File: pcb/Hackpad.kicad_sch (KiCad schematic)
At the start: 21 parts, among them SW1 SW_Push, SW10 RotaryEncoder, SW2 SW_Push, SW3 SW_Push, SW4 SW_Push, SW5 SW_Push, SW6 SW_Push, SW7 SW_Push, SW8 SW_Push, SW9 SW_Push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

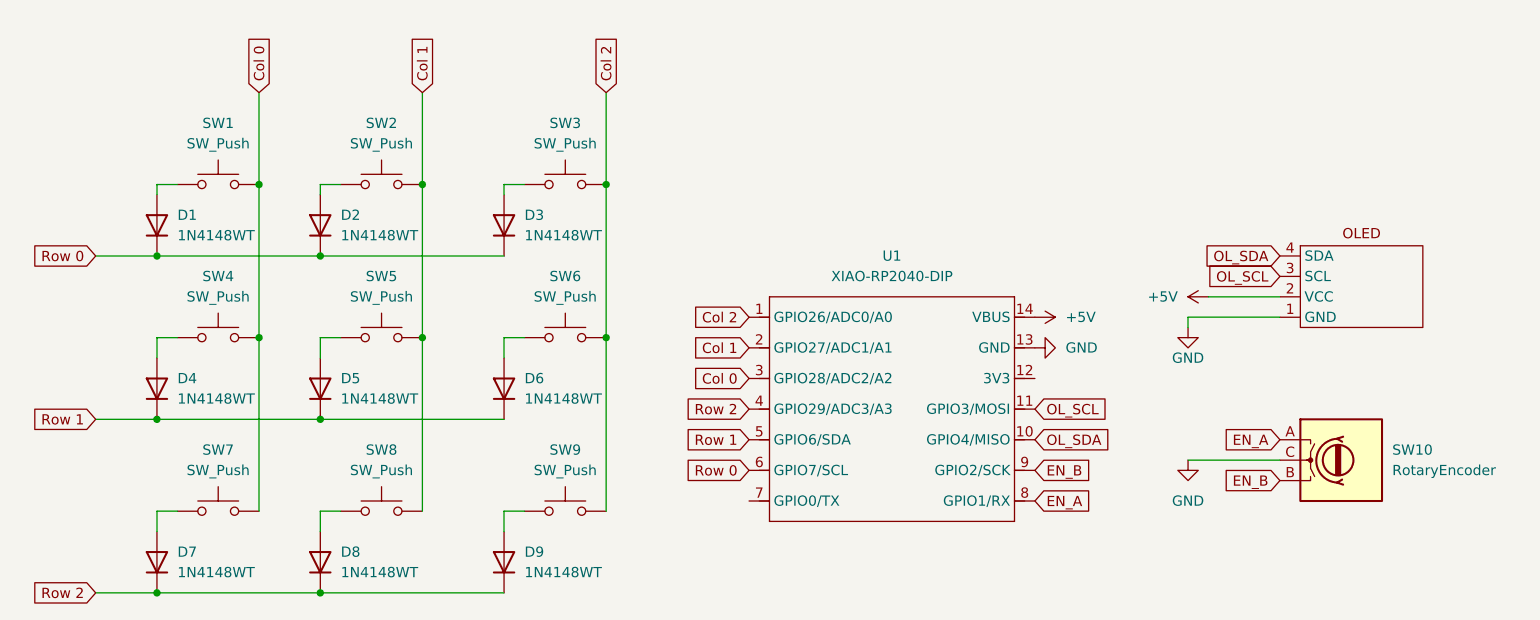
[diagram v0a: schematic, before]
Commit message: fix OLED schematic and pcb OLED wiring
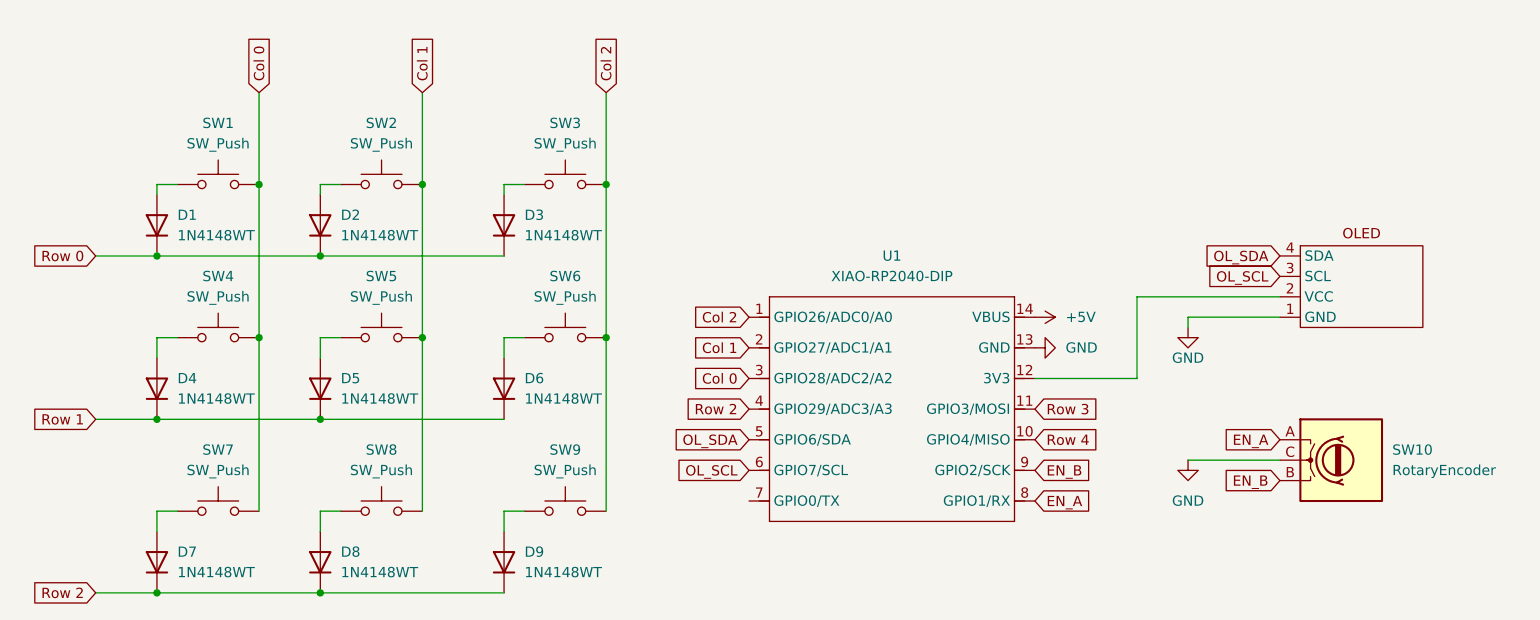
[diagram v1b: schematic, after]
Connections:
- net +5V: no longer U2.2 (VCC)
- net OL_SCL: now also U1.6 (GPIO7/SCL); no longer U1.11 (GPIO3/MOSI)
- net OL_SDA: now also U1.5 (GPIO6/SDA); no longer U1.10 (GPIO4/MISO)
- net Row 0: no longer U1.6 (GPIO7/SCL)
- net Row 1: no longer U1.5 (GPIO6/SDA)
- net at U1.12 (3V3): now also U2.2 (VCC)
- new net Row 3: U1.11 (GPIO3/MOSI)
- new net Row 4: U1.10 (GPIO4/MISO)

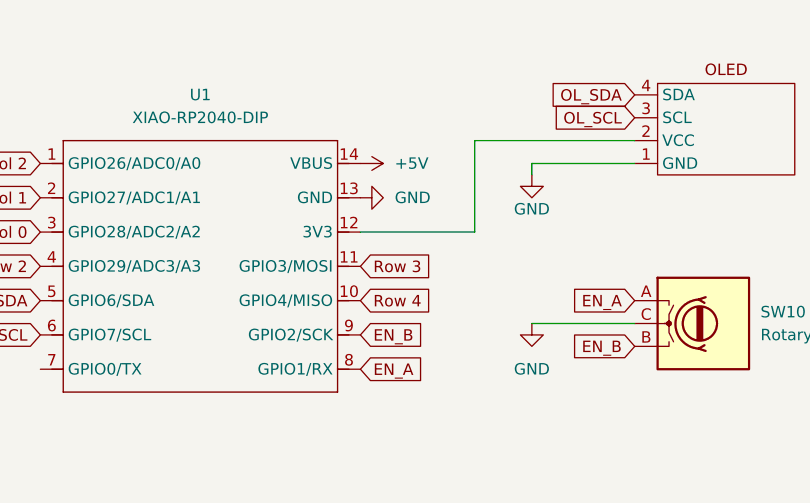
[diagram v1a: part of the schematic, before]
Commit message: fix matrix wiring issue
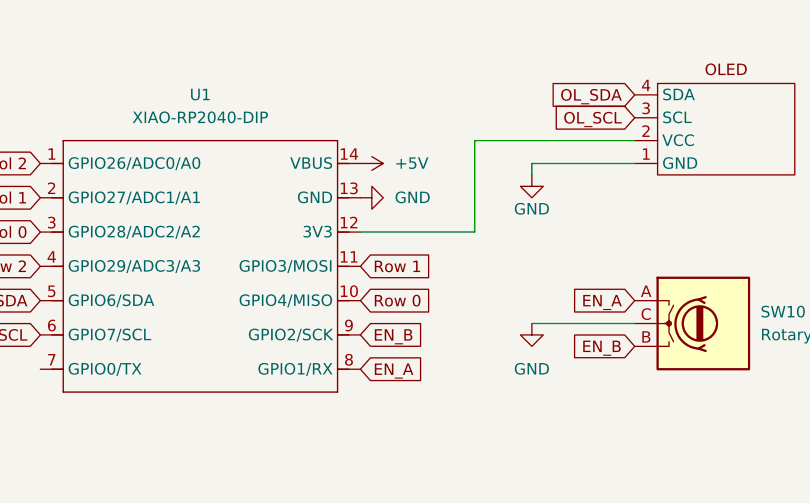
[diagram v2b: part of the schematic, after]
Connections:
- net Row 3 is gone; now on net Row 1: U1.11 (GPIO3/MOSI)
- net Row 4 is gone; now on net Row 0: U1.10 (GPIO4/MISO)
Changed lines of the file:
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@@
 		)
 	)
-	(global_label "Row 4"
+	(global_label "Row 0"
 		(shape input)
 		(at 185.42 101.6 0)
@@
 		)
 	)
-	(global_label "Row 3"
+	(global_label "Row 1"
 		(shape input)
 		(at 185.42 97.79 0)
